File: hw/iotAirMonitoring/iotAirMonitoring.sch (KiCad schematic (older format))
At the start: 57 parts, among them J4 PROGRAMMER, J6 EN_3V3_PROGRAMMER, Q1 MMBT3904, Q14 AO3401A, Q15 2N7002, Q2 MMBT3904, SW1 PWR_ON, SW2 PWR_OFF, SW3 RESET, SW4 SW_Push, U1 ESP32-WROOM-32, U2 MCP3202-BI/SN, U5 RFM95W-868S2

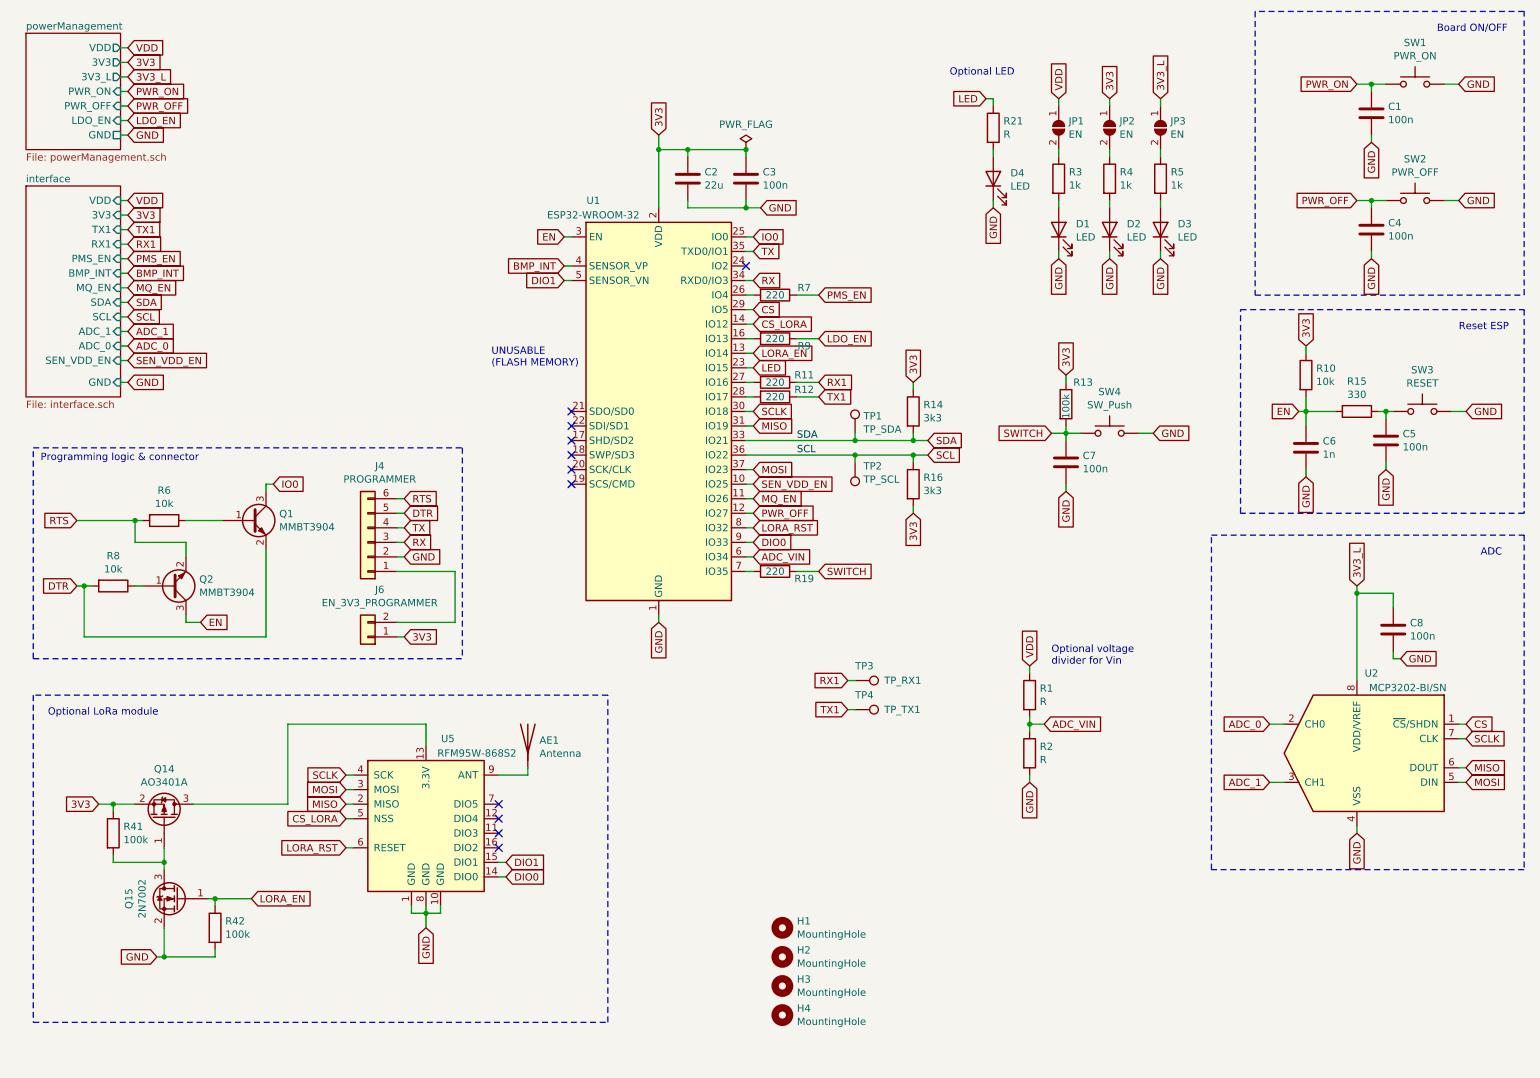
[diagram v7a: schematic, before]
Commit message: First version routed main board
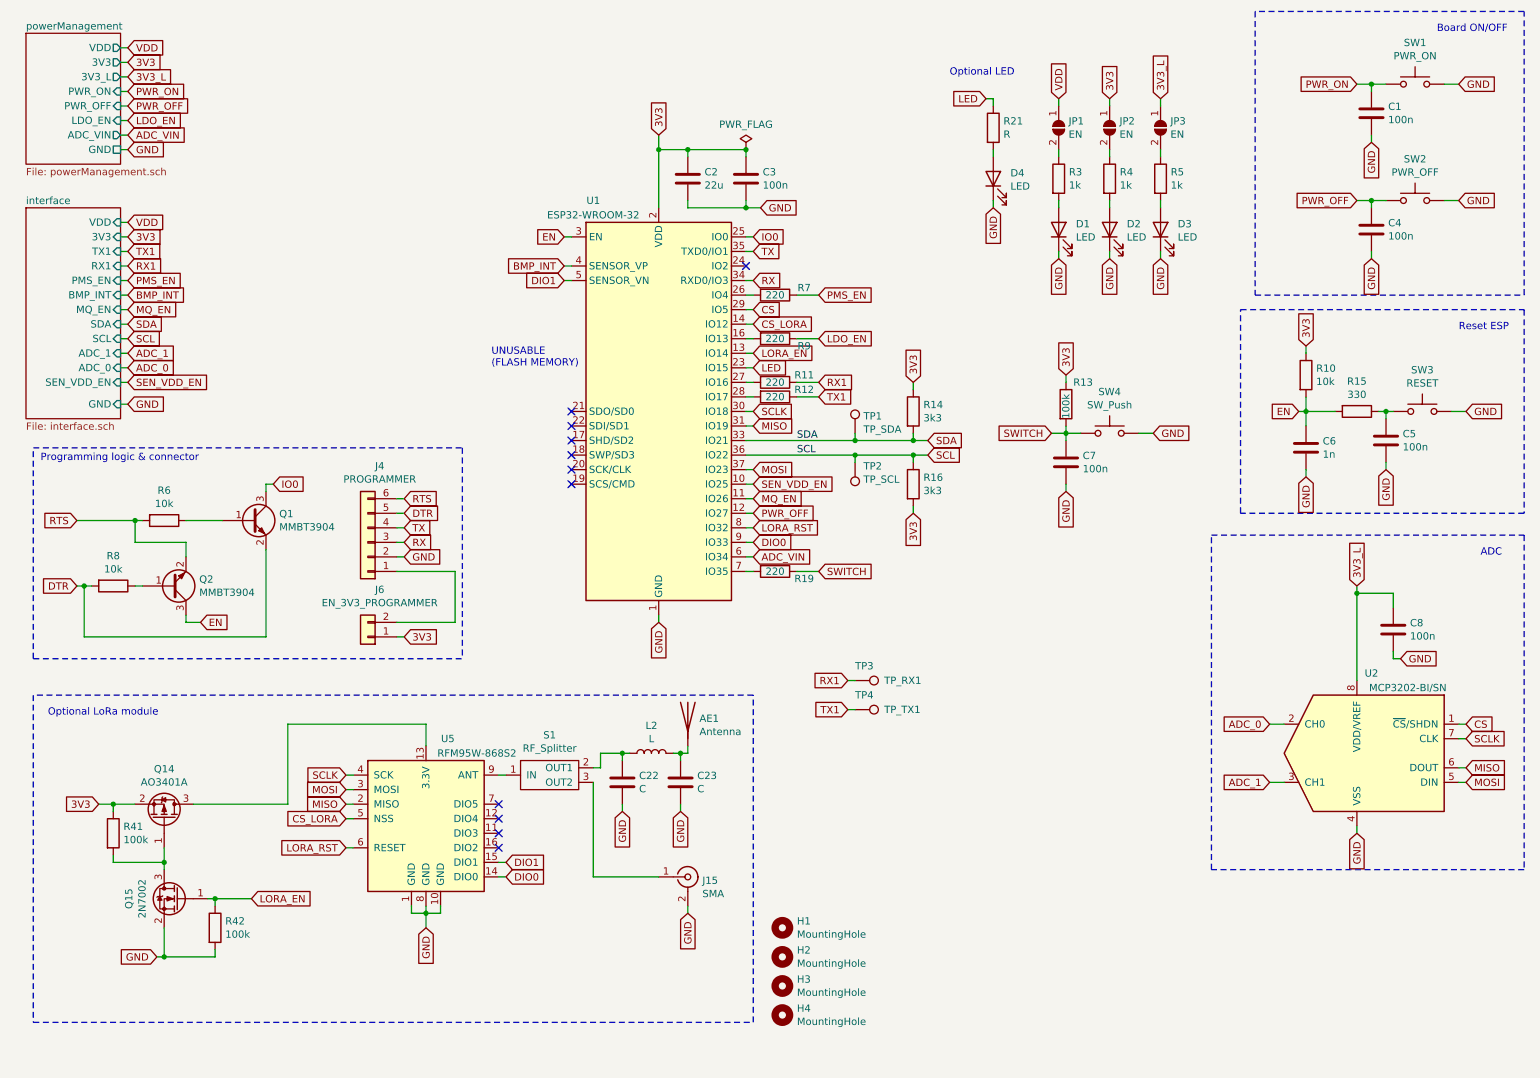
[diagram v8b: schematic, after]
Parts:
- removed R1, R2: R, Resistor_SMD:R_0805_2012Metric_Pad1.20x1.40mm_HandSolder, symbol Device:R
- added C22, C23: C, Capacitor_SMD:C_0805_2012Metric_Pad1.18x1.45mm_HandSolder, symbol Device:C
- added J15: SMA, Connector_Coaxial:SMA_Samtec_SMA-J-P-X-ST-EM1_EdgeMount, symbol Connector:Conn_Coaxial
- added L2: L, Inductor_SMD:L_0805_2012Metric_Pad1.05x1.20mm_HandSolder, symbol Device:L
- added S1: RF_Splitter, iotAirMonitoring:RF_Splitter, symbol iotAirMonitoring:RF_Splitter
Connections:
- net GND: now also C22.2, C23.2, J15.2 (Ext)
- net at AE1.1 (A): now also C23.1, L2.2; no longer U5.9 (ANT)
- new net: J15.1 (In), S1.3 (OUT2)
- new net: C22.1, L2.1, S1.2 (OUT1)
- new net: S1.1 (IN), U5.9 (ANT)
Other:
- note removed: "Optional voltage\ndivider for Vin"
- moved on the sheet: AE1
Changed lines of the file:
@@
 Comment4 ""
 $EndDescr
-$Sheet
-S 750  700  650  800
-U 61767442
-F0 "powerManagement" 50
-F1 "powerManagement.sch" 50
-F2 "GND" U R 1400 1400 50
-F3 "PWR_ON" I R 1400 1100 50
-F4 "PWR_OFF" I R 1400 1200 50
-F5 "VDD" O R 1400 800 50
-F6 "3V3_L" O R 1400 1000 50
-F7 "3V3" O R 1400 900 50
-F8 "LDO_EN" I R 1400 1300 50
-$EndSheet
 Text GLabel 1450 800  2    50   Input ~ 0
 VDD
@@
 Text GLabel 1450 1200 2    50   Input ~ 0
 PWR_OFF
-Text GLabel 1450 1400 2    50   Input ~ 0
+Text GLabel 1450 1500 2    50   Input ~ 0
 GND
 Text GLabel 1450 1000 2    50   Input ~ 0
@@
 Text Notes 850  3650 0    50   ~ 0
 Programming logic & connector
-$Comp
-L Device:R R1
-U 1 1 618EBDFB
-P 7650 5250
-F 0 "R1" H 7720 5296 50  0000 L CNN
-F 1 "R" H 7720 5205 50  0000 L CNN
-F 2 "Resistor_SMD:R_0805_2012Metric_Pad1.20x1.40mm_HandSolder" V 7580 5250 50  0001 C CNN
-F 3 "~" H 7650 5250 50  0001 C CNN
-	1    7650 5250
-	1    0    0    -1
-$EndComp
-$Comp
-L Device:R R2
-U 1 1 618EC174
-P 7650 5650
-F 0 "R2" H 7720 5696 50  0000 L CNN
-F 1 "R" H 7720 5605 50  0000 L CNN
-F 2 "Resistor_SMD:R_0805_2012Metric_Pad1.20x1.40mm_HandSolder" V 7580 5650 50  0001 C CNN
-F 3 "~" H 7650 5650 50  0001 C CNN
-	1    7650 5650
-	1    0    0    -1
-$EndComp
-Wire Wire Line
-	7650 5400 7650 5450
-Wire Wire Line
-	7650 5450 7750 5450
-Connection ~ 7650 5450
-Wire Wire Line
-	7650 5450 7650 5500
-Text GLabel 7750 5450 2    50   Input ~ 0
-ADC_VIN
-Wire Wire Line
-	7650 5100 7650 5050
-Wire Wire Line
-	7650 5800 7650 5850
 Wire Wire Line
 	5700 4300 5750 4300
 Text GLabel 5750 4300 2    50   Input ~ 0
 ADC_VIN
-Text Notes 7800 5050 0    50   ~ 0
-Optional voltage\ndivider for Vin
 $Comp
 L Switch:SW_Push SW4
@@
 	1400 800  1450 800
 Wire Wire Line
-	1400 1400 1450 1400
-Wire Wire Line
 	1450 1300 1400 1300
 Wire Wire Line
@@
 Wire Wire Line
 	1450 1100 1400 1100
-Text GLabel 7650 5050 1    50   Input ~ 0
-VDD
-Text GLabel 7650 5850 3    50   Input ~ 0
-GND
 Text GLabel 5100 1400 1    50   Input ~ 0
 3V3
@@
 L Device:Antenna AE1
 U 1 1 61B559CE
-P 4200 5550
-F 0 "AE1" H 4280 5539 50  0000 L CNN
-F 1 "Antenna" H 4280 5448 50  0000 L CNN
-F 2 "RF_Antenna:Texas_SWRA416_868MHz_915MHz" H 4200 5550 50  0001 C CNN
-F 3 "~" H 4200 5550 50  0001 C CNN
-	1    4200 5550
-	1    0    0    -1
-$EndComp
-Wire Wire Line
-	4000 5800 4200 5800
-Wire Wire Line
-	4200 5800 4200 5750
+P 5300 5400
+F 0 "AE1" H 5380 5389 50  0000 L CNN
+F 1 "Antenna" H 5380 5298 50  0000 L CNN
+F 2 "RF_Antenna:Texas_SWRA416_868MHz_915MHz" H 5300 5400 50  0001 C CNN
+F 3 "~" H 5300 5400 50  0001 C CNN
+	1    5300 5400
+	1    0    0    -1
+$EndComp
 Wire Notes Line
 	800  3550 3750 3550
@@
 Text GLabel 5750 4100 2    50   Input ~ 0
 LORA_RST
-$Sheet
-S 750  1750 650  1450
-U 61D2D467
-F0 "interface" 50
-F1 "interface.sch" 50
-F2 "TX1" I R 1400 2050 50
-F3 "RX1" I R 1400 2150 50
-F4 "GND" I R 1400 3100 50
-F5 "3V3" I R 1400 1950 50
-F6 "BMP_INT" I R 1400 2350 50
-F7 "SDA" I R 1400 2550 50
-F8 "SCL" I R 1400 2650 50
-F9 "ADC_1" I R 1400 2750 50
-F10 "ADC_0" I R 1400 2850 50
-F11 "PMS_EN" I R 1400 2250 50
-F12 "VDD" I R 1400 1850 50
-F13 "SEN_VDD_EN" I R 1400 2950 50
-F14 "MQ_EN" I R 1400 2450 50
-$EndSheet
 Wire Wire Line
 	3300 4850 3350 4850
@@
 	800  5250 800  7500
 Wire Notes Line
-	800  7500 4750 7500
-Wire Notes Line
-	4750 7500 4750 5250
-Wire Notes Line
-	4750 5250 800  5250
+	800  7500 5750 7500
+Wire Notes Line
+	5750 7500 5750 5250
+Wire Notes Line
+	5750 5250 800  5250
 Text Notes 900  5400 0    50   ~ 0
 Optional LoRa module
-Wire Wire Line
-	1400 1850 1450 1850
-Wire Wire Line
-	1450 1950 1400 1950
-Wire Wire Line
-	1450 2050 1400 2050
-Wire Wire Line
-	1450 2150 1400 2150
-Wire Wire Line
-	1450 2250 1400 2250
-Wire Wire Line
-	1450 2350 1400 2350
-Wire Wire Line
-	1450 2450 1400 2450
-Wire Wire Line
-	1450 2550 1400 2550
-Wire Wire Line
-	1450 2650 1400 2650
-Wire Wire Line
-	1450 2750 1400 2750
-Wire Wire Line
-	1450 2850 1400 2850
-Wire Wire Line
-	1450 2950 1400 2950
-Wire Wire Line
-	1450 3100 1400 3100
-Text GLabel 1450 1850 2    50   Input ~ 0
-VDD
-Text GLabel 1450 1950 2    50   Input ~ 0
-3V3
-Text GLabel 1450 2050 2    50   Input ~ 0
-TX1
-Text GLabel 1450 2150 2    50   Input ~ 0
-RX1
-Text GLabel 1450 2250 2    50   Input ~ 0
-PMS_EN
-Text GLabel 1450 2350 2    50   Input ~ 0
-BMP_INT
-Text GLabel 1450 2450 2    50   Input ~ 0
-MQ_EN
-Text GLabel 1450 2550 2    50   Input ~ 0
-SDA
-Text GLabel 1450 2650 2    50   Input ~ 0
-SCL
-Text GLabel 1450 2750 2    50   Input ~ 0
-ADC_1
-Text GLabel 1450 2850 2    50   Input ~ 0
-ADC_0
-Text GLabel 1450 2950 2    50   Input ~ 0
-SEN_VDD_EN
-Text GLabel 1450 3100 2    50   Input ~ 0
-GND
 $Comp
 L Connector:TestPoint TP3
@@
 Text GLabel 6400 5350 0    50   Input ~ 0
 TX1
+Text GLabel 1450 3250 2    50   Input ~ 0
+GND
+Text GLabel 1450 3100 2    50   Input ~ 0
+SEN_VDD_EN
+Text GLabel 1450 3000 2    50   Input ~ 0
+ADC_0
+Text GLabel 1450 2900 2    50   Input ~ 0
+ADC_1
+Text GLabel 1450 2800 2    50   Input ~ 0
+SCL
+Text GLabel 1450 2700 2    50   Input ~ 0
+SDA
+Text GLabel 1450 2600 2    50   Input ~ 0
+MQ_EN
+Text GLabel 1450 2500 2    50   Input ~ 0
+BMP_INT
+Text GLabel 1450 2400 2    50   Input ~ 0
+PMS_EN
+Text GLabel 1450 2300 2    50   Input ~ 0
+RX1
+Text GLabel 1450 2200 2    50   Input ~ 0
+TX1
+Text GLabel 1450 2100 2    50   Input ~ 0
+3V3
+Text GLabel 1450 2000 2    50   Input ~ 0
+VDD
+Wire Wire Line
+	1450 3250 1400 3250
+Wire Wire Line
+	1450 3100 1400 3100
+Wire Wire Line
+	1450 3000 1400 3000
+Wire Wire Line
+	1450 2900 1400 2900
+Wire Wire Line
+	1450 2800 1400 2800
+Wire Wire Line
+	1450 2700 1400 2700
+Wire Wire Line
+	1450 2600 1400 2600
+Wire Wire Line
+	1450 2500 1400 2500
+Wire Wire Line
+	1450 2400 1400 2400
+Wire Wire Line
+	1450 2300 1400 2300
+Wire Wire Line
+	1450 2200 1400 2200
+Wire Wire Line
+	1450 2100 1400 2100
+Wire Wire Line
+	1400 2000 1450 2000
+$Sheet
+S 750  1900 650  1450
+U 61D2D467
+F0 "interface" 50
+F1 "interface.sch" 50
+F2 "TX1" I R 1400 2200 50
+F3 "RX1" I R 1400 2300 50
+F4 "GND" I R 1400 3250 50
+F5 "3V3" I R 1400 2100 50
+F6 "BMP_INT" I R 1400 2500 50
+F7 "SDA" I R 1400 2700 50
+F8 "SCL" I R 1400 2800 50
+F9 "ADC_1" I R 1400 2900 50
+F10 "ADC_0" I R 1400 3000 50
+F11 "PMS_EN" I R 1400 2400 50
+F12 "VDD" I R 1400 2000 50
+F13 "SEN_VDD_EN" I R 1400 3100 50
+F14 "MQ_EN" I R 1400 2600 50
+$EndSheet
+$Sheet
+S 750  700  650  900
+U 61767442
+F0 "powerManagement" 50
+F1 "powerManagement.sch" 50
+F2 "GND" U R 1400 1500 50
+F3 "PWR_ON" I R 1400 1100 50
+F4 "PWR_OFF" I R 1400 1200 50
+F5 "VDD" O R 1400 800 50
+F6 "3V3_L" O R 1400 1000 50
+F7 "3V3" O R 1400 900 50
+F8 "LDO_EN" I R 1400 1300 50
+F9 "ADC_VIN" O R 1400 1400 50
+$EndSheet
+Wire Wire Line
+	1450 1500 1400 1500
+Wire Wire Line
+	1400 1400 1450 1400
+Text GLabel 1450 1400 2    50   Input ~ 0
+ADC_VIN
+$Comp
+L Connector:Conn_Coaxial J15
+U 1 1 618F4FB3
+P 5300 6500
+F 0 "J15" H 5400 6475 50  0000 L CNN
+F 1 "SMA" H 5400 6384 50  0000 L CNN
+F 2 "Connector_Coaxial:SMA_Samtec_SMA-J-P-X-ST-EM1_EdgeMount" H 5300 6500 50  0001 C CNN
+F 3 "https://www.tme.eu/Document/b4dd5925cecd78bf6385fa91265dd943/RF2-145A-T-17-50-G-HDW.pdf" H 5300 6500 50  0001 C CNN
+	1    5300 6500
+	1    0    0    -1
+$EndComp
+Text GLabel 5300 6750 3    50   Input ~ 0
+GND
+Wire Wire Line
+	5300 6750 5300 6700
+$Comp
+L Device:L L2
+U 1 1 6193ABDB
+P 5050 5650
+F 0 "L2" V 5240 5650 50  0000 C CNN
+F 1 "L" V 5149 5650 50  0000 C CNN
+F 2 "Inductor_SMD:L_0805_2012Metric_Pad1.05x1.20mm_HandSolder" H 5050 5650 50  0001 C CNN
+F 3 "~" H 5050 5650 50  0001 C CNN
+	1    5050 5650
+	0    -1   -1   0
+$EndComp
+$Comp
+L Device:C C22
+U 1 1 6193B857
+P 4850 5850
+F 0 "C22" H 4965 5896 50  0000 L CNN
+F 1 "C" H 4965 5805 50  0000 L CNN
+F 2 "Capacitor_SMD:C_0805_2012Metric_Pad1.18x1.45mm_HandSolder" H 4888 5700 50  0001 C CNN
+F 3 "~" H 4850 5850 50  0001 C CNN
+	1    4850 5850
+	1    0    0    -1
+$EndComp
+$Comp
+L Device:C C23
+U 1 1 6193B9A0
+P 5250 5850
+F 0 "C23" H 5365 5896 50  0000 L CNN
+F 1 "C" H 5365 5805 50  0000 L CNN
+F 2 "Capacitor_SMD:C_0805_2012Metric_Pad1.18x1.45mm_HandSolder" H 5288 5700 50  0001 C CNN
+F 3 "~" H 5250 5850 50  0001 C CNN
+	1    5250 5850
+	1    0    0    -1
+$EndComp
+Text GLabel 4850 6050 3    50   Input ~ 0
+GND
+Text GLabel 5250 6050 3    50   Input ~ 0
+GND
+Wire Wire Line
+	5250 6050 5250 6000
+Wire Wire Line
+	4850 6050 4850 6000
+Wire Wire Line
+	4850 5700 4850 5650
+Wire Wire Line
+	4850 5650 4900 5650
+Wire Wire Line
+	5250 5700 5250 5650
+Wire Wire Line
+	5250 5650 5200 5650
+Wire Wire Line
+	5250 5650 5300 5650
+Wire Wire Line
+	5300 5650 5300 5600
+Connection ~ 5250 5650
+Wire Wire Line
+	4850 5650 4700 5650
+Connection ~ 4850 5650
+$Comp
+L iotAirMonitoring:RF_Splitter S1
+U 1 1 619D7D18
+P 4350 5800
+F 0 "S1" H 4350 6075 50  0000 C CNN
+F 1 "RF_Splitter" H 4350 5984 50  0000 C CNN
+F 2 "iotAirMonitoring:RF_Splitter" H 4350 5800 50  0001 C CNN
+F 3 "" H 4350 5800 50  0001 C CNN
+	1    4350 5800
+	1    0    0    -1
+$EndComp
+Wire Wire Line
+	4000 5800 4050 5800
+Wire Wire Line
+	4650 5750 4700 5750
+Wire Wire Line
+	4700 5750 4700 5650
+Wire Wire Line
+	4650 5850 4650 6500
+Wire Wire Line
+	4650 6500 5100 6500
 $EndSCHEMATC
